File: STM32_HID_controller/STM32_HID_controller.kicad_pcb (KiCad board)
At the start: 2 copper layers, 249.9 x 110.4 mm, 49 parts, among them J1 USB_B_Micro, J2 Conn_01x04_Pin, J3 Conn_01x03_Pin, J5 Conn_01x03_Pin, SW1 SW_SPDT, SW10 SW_Push, SW11 SW_Push, SW14 SW_Push, SW2 SW_Push, SW3 SW_Push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

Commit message: Started flux
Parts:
- moved C6 4.89 mm to (149.2, 47.3), turned to 180 degrees
- moved C4 1.53 mm to (162.1, 41.3)
- moved C2 1.00 mm to (150.1, 29.5)
- moved C1 0.96 mm to (145.9, 40.7)
- moved C12 0.96 mm to (154.4, 49.7)
- moved C18 0.96 mm to (165.9, 37.7)
- moved C7 0.96 mm to (155.4, 45.2)
- moved FB1 0.96 mm to (159.7, 44.2)
- moved C10 0.96 mm to (165.4, 43.2)
- moved C15 0.96 mm to (156.9, 51.7)
- moved C16 0.96 mm to (159.9, 51.7)
- moved C17 0.96 mm to (165.9, 39.7)
- moved C3 0.96 mm to (161.4, 33.7)
- moved C5 0.96 mm to (149.4, 45.1)
- moved C8 0.96 mm to (157.9, 46.2)
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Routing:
- net vly: track 0.00 -> 78.6 mm
- net /SW_BOOT0: track 0.00 -> 21.1 mm
- net /SWDIO: track 0.00 -> 18.9 mm
- net /SWCLK: track 0.00 -> 16.7 mm
- net GND: track 0.00 -> 14.6 mm
- net +3.3V: track 0.00 -> 14.1 mm
- net /HSE_IN: track 0.00 -> 12.8 mm
- net /HSE_OUT: track 0.00 -> 9.72 mm
- net /USB_D-: track 0.00 -> 9.57 mm
- net /USB_D+: track 0.00 -> 9.49 mm
- net /BOOT0: track 0.00 -> 8.09 mm
- net vry: track 0.00 -> 6.77 mm
- net vrx: track 0.00 -> 6.19 mm
- net +3.3VA: track 0.00 -> 2.14 mm
- added copper zone on B.Cu, net GND

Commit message: Started flux
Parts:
- moved U4 159.0 mm to (218.8, 100.1)
- moved U5 153.6 mm to (70.1, 62.9)
- moved C16 20.5 mm to (141.7, 42.5), turned to 90 degrees
- moved SW1 18.1 mm to (133.9, 37.1), turned to -90 degrees
- moved C15 16.2 mm to (141.7, 46.1)
- moved C10 13.5 mm to (152.9, 48.4), turned to 0 degrees
- moved FB1 5.14 mm to (157.9, 49.0)
- moved C9 5.05 mm to (158.1, 50.9), turned to 0 degrees
- moved C11 2.63 mm to (149.3, 50.0)
- moved C12 2.63 mm to (151.8, 49.9)
- moved Y1 2.63 mm to (150.7, 53.0)
- moved U2 2.19 mm to (172.3, 30.8), turned to -90 degrees
- moved C5 2.18 mm to (147.3, 45.3)
- moved C6 2.18 mm to (147.0, 47.4)
- moved C8 1.39 mm to (157.0, 47.2), turned to 0 degrees
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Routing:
- net SCL: track 0.00 -> 315.1 mm
- net cs: track 0.00 -> 304.6 mm
- net jl: track 0.00 -> 214.3 mm
- net jr: track 0.00 -> 151.6 mm
- net vlx: track 0.00 -> 123.3 mm
- net vrx: track 6.19 -> 119.7 mm
- net zl: track 0.00 -> 102.6 mm
- net unconnected-(U1-PB7-Pad59): track 0.00 -> 92.6 mm
- net /A: track 0.00 -> 92.1 mm
- net /Y: track 0.00 -> 90.7 mm
- net /X: track 0.00 -> 88.1 mm
- net vry: track 6.77 -> 93.4 mm
- net r: track 0.00 -> 78.9 mm
- net SDO: track 0.00 -> 67.0 mm
- net SDI: track 0.00 -> 62.3 mm
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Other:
- outline, holes or cut-outs redrawn

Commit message: Started flux for left and right
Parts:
- removed R3: 10k, Resistor_SMD:R_0402_1005Metric
- removed U3: ADXL345, ADXL345:PQFN80P500X300X100-14N
- added U6: ADXL343, Package_LGA:LGA-14_3x5mm_P0.8mm_LayoutBorder1x6y, F.Cu at (112.2, 56.1)
- moved H2 14.3 mm to (51.1, 115.1)
- moved H4 12.5 mm to (51.1, 22.1)
- moved H6 7.00 mm to (277.1, 115.1)
- moved C17 5.70 mm to (164.2, 45.7)
- moved SW14 4.87 mm to (150.6, 69.8)
- moved C18 4.79 mm to (164.3, 42.6)
- moved C7 3.28 mm to (158.7, 45.6)
- moved C8 1.83 mm to (158.8, 47.1)
- moved C9 1.83 mm to (159.9, 50.8)
- moved FB1 1.83 mm to (159.7, 48.9)
- moved C1 1.33 mm to (145.0, 41.6)
- moved C4 0.90 mm to (161.5, 42.0)
- moved SW1 0.71 mm to (134.4, 36.6)
- moved C5 0.59 mm to (147.1, 44.8)
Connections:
- SW10 pad 1: /+ -> +
- SW11 pad 1: /- -> -
- SW14 pad 1: /ACC_control -> ACC_control
- SW2 pad 2: /home -> home
- SW3 pad 2: /capture -> capture
- SW6 pad 1: /A -> A
- SW7 pad 1: /B -> B
- SW8 pad 1: /X -> X
- SW9 pad 1: /Y -> Y
- U1 pad 11: unconnected-(U1-PC3-Pad11) -> cs
- U1 pad 22: cs -> jr
- U1 pad 23: unconnected-(U1-PA7-Pad23) -> B
- U1 pad 24: unconnected-(U1-PC4-Pad24) -> Y
- U1 pad 25: unconnected-(U1-PC5-Pad25) -> A
- U1 pad 26: unconnected-(U1-PB0-Pad26) -> X
- U1 pad 27: unconnected-(U1-PB1-Pad27) -> r
- U1 pad 28: unconnected-(U1-PB2-Pad28) -> zr
- U1 pad 29: SCL -> unconnected-(U1-PB10-Pad29)
- U1 pad 34: unconnected-(U1-PB13-Pad34) -> SCL
- U1 pad 35: l -> unconnected-(U1-PB14-Pad35)
- U1 pad 36: /ACC_control -> unconnected-(U1-PB15-Pad36)
- U1 pad 37: /home -> unconnected-(U1-PC6-Pad37)
- U1 pad 38: /capture -> unconnected-(U1-PC7-Pad38)
- U1 pad 39: zr -> unconnected-(U1-PC8-Pad39)
- U1 pad 40: zl -> unconnected-(U1-PC9-Pad40)
- U1 pad 41: jr -> unconnected-(U1-PA8-Pad41)
- U1 pad 42: jl -> unconnected-(U1-PA9-Pad42)
- U1 pad 43: r -> unconnected-(U1-PA10-Pad43)
- U1 pad 51: unconnected-(U1-PC10-Pad51) -> l
- U1 pad 52: unconnected-(U1-PC11-Pad52) -> zl
- U1 pad 55: /A -> jl
- U1 pad 56: /B -> home
- U1 pad 57: /X -> +
- U1 pad 58: /Y -> unconnected-(U1-PB6-Pad58)
- U1 pad 61: /+ -> -
- U1 pad 62: /- -> capture
- U1 pad 8: unconnected-(U1-PC0-Pad8) -> ACC_control
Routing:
- net +: track 0.00 -> 293.3 mm
- net home: track 0.00 -> 273.7 mm
- net capture: track 0.00 -> 238.1 mm
- net -: track 0.00 -> 231.8 mm
- net cs: track 304.6 -> 78.2 mm
- net SCL: track 315.1 -> 530.5 mm
- net jl: track 214.3 -> 103.3 mm
- net A: track 0.00 -> 110.2 mm
- net B: track 0.00 -> 96.3 mm
- net unconnected-(U1-PB7-Pad59): track 92.6 -> 0.00 mm
- net /A: track 92.1 -> 0.00 mm
- net /Y: track 90.7 -> 0.00 mm
- net /X: track 88.1 -> 0.00 mm
- net X: track 0.00 -> 82.9 mm
- net jr: track 151.6 -> 82.3 mm
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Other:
- board size 249.9 x 110.4 mm -> 237.3 x 103.7 mm

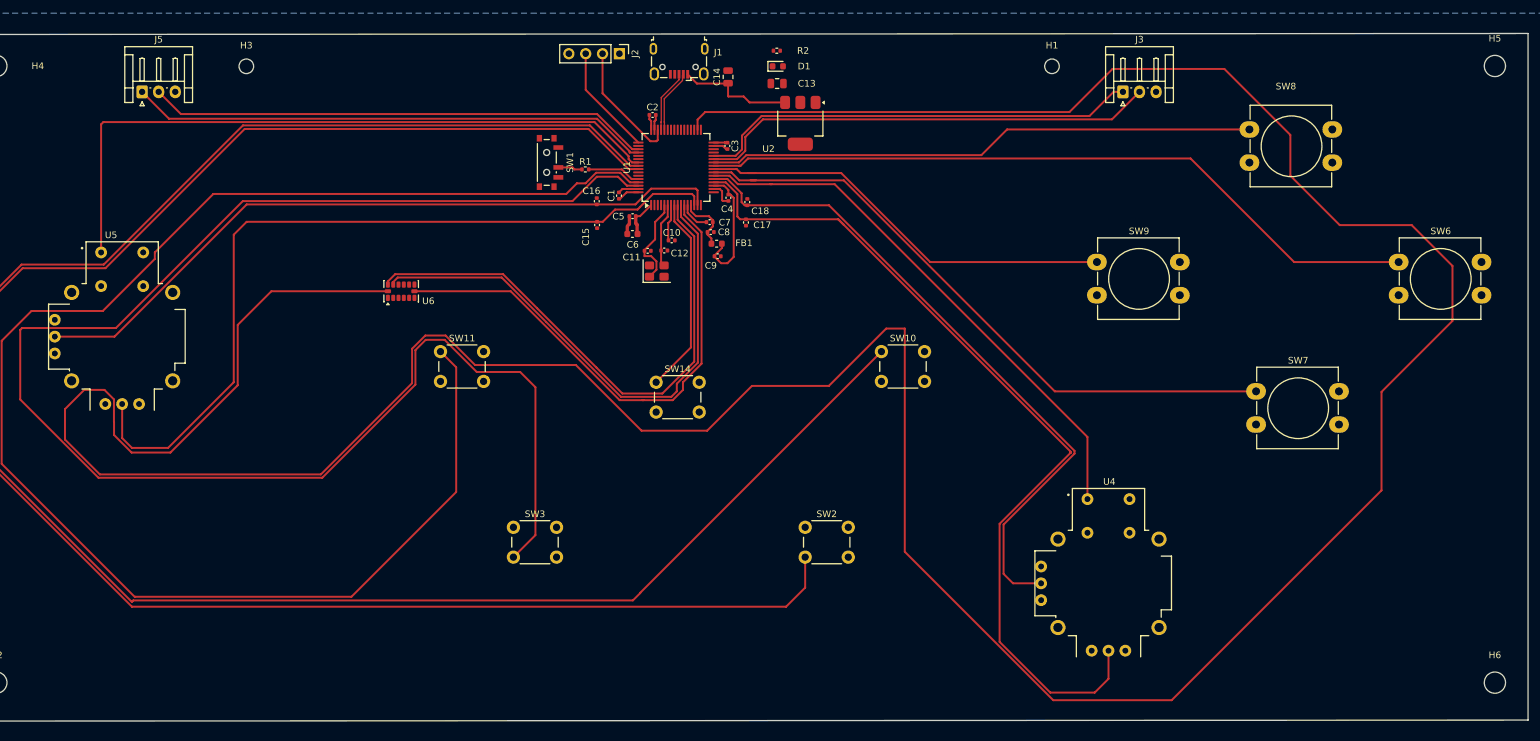
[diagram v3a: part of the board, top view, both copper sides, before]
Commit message: added gnd vias shortend sclk
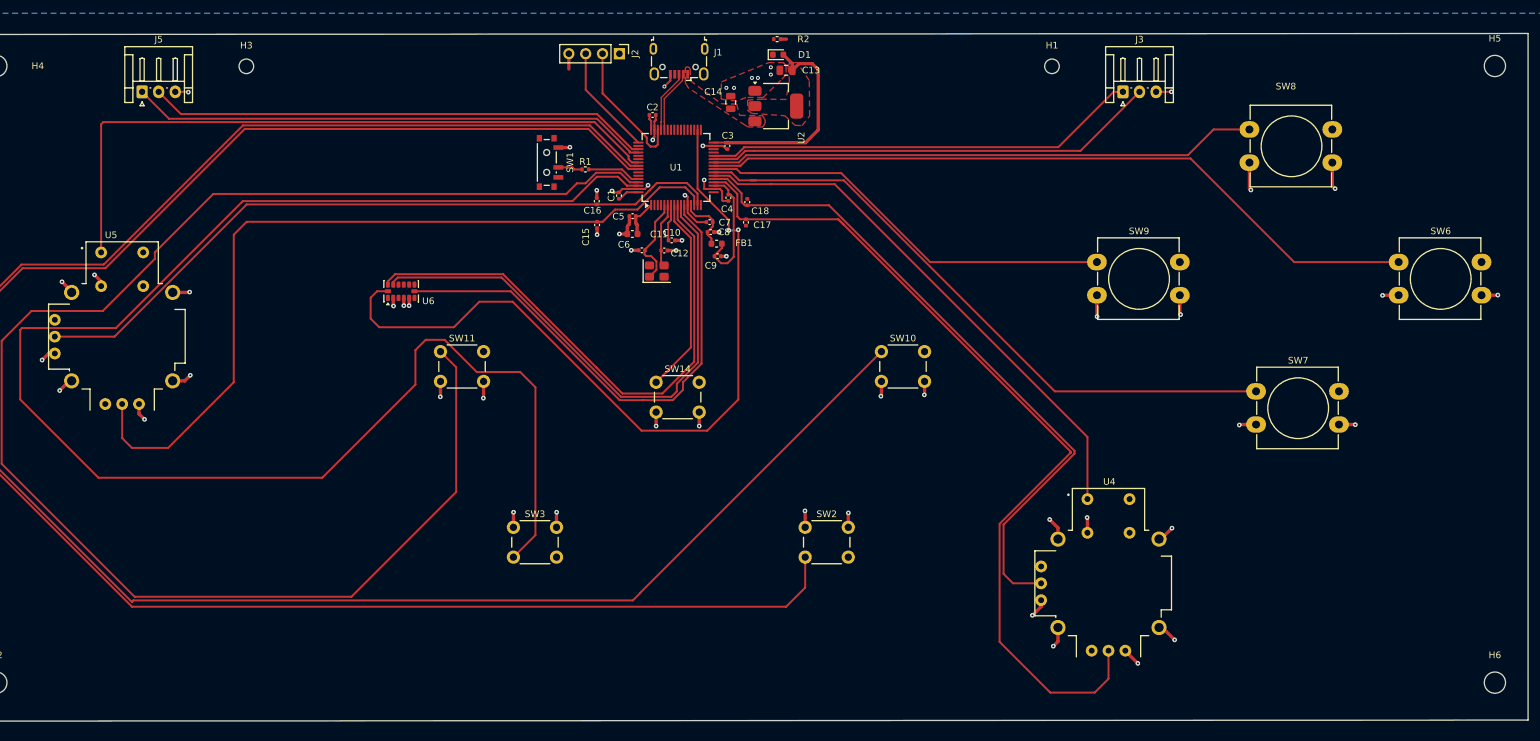
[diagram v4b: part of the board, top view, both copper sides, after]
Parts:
- moved U2 4.52 mm to (168.7, 28.1), turned to 0 degrees
- moved C14 3.87 mm to (161.8, 27.6)
- moved C13 2.41 mm to (170.2, 22.8)
- moved D1 1.75 mm to (169.0, 20.4)
- moved R2 1.75 mm to (168.8, 18.1)
- moved C11 0.88 mm to (148.4, 49.9), turned to 180 degrees
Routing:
- net SCL: track 530.5 -> 118.0 mm, vias 0 -> 2
- net GND: track 18.9 -> 137.8 mm, vias 0 -> 59
- net +3.3V: track 32.9 -> 64.5 mm
- net VBUS: track 17.6 -> 0.00 mm
- net /SWDIO: track 18.9 -> 20.4 mm
- net r: track 69.7 -> 68.4 mm
- net zr: track 66.9 -> 65.7 mm
- net vlx: track 122.4 -> 123.2 mm
- added copper zone on F.Cu, net +3.3V
- added copper zone on F.Cu, net GND
- added copper zone on F.Cu, net VBUS

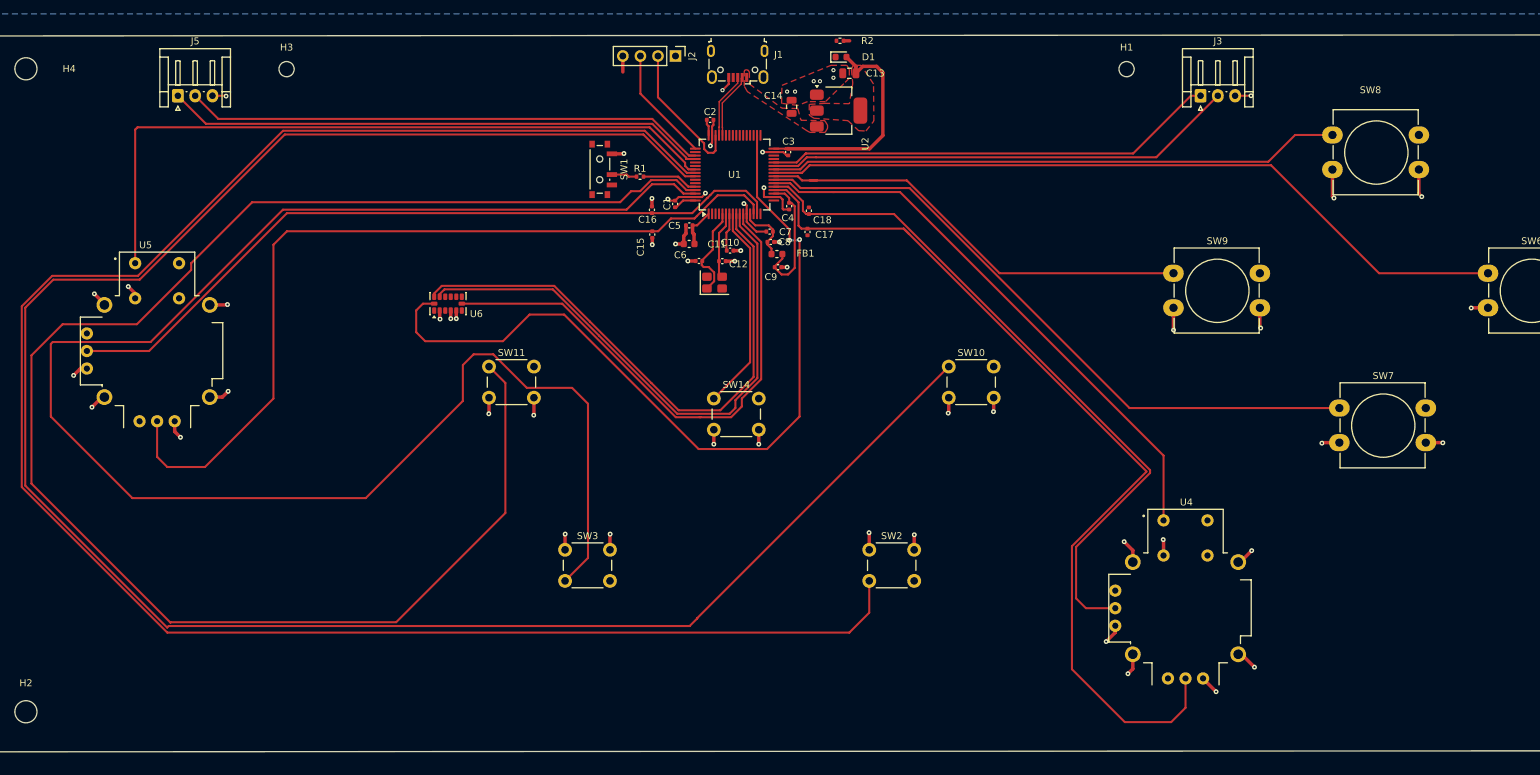
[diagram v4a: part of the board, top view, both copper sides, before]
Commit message: added gnd vias shortend sclk
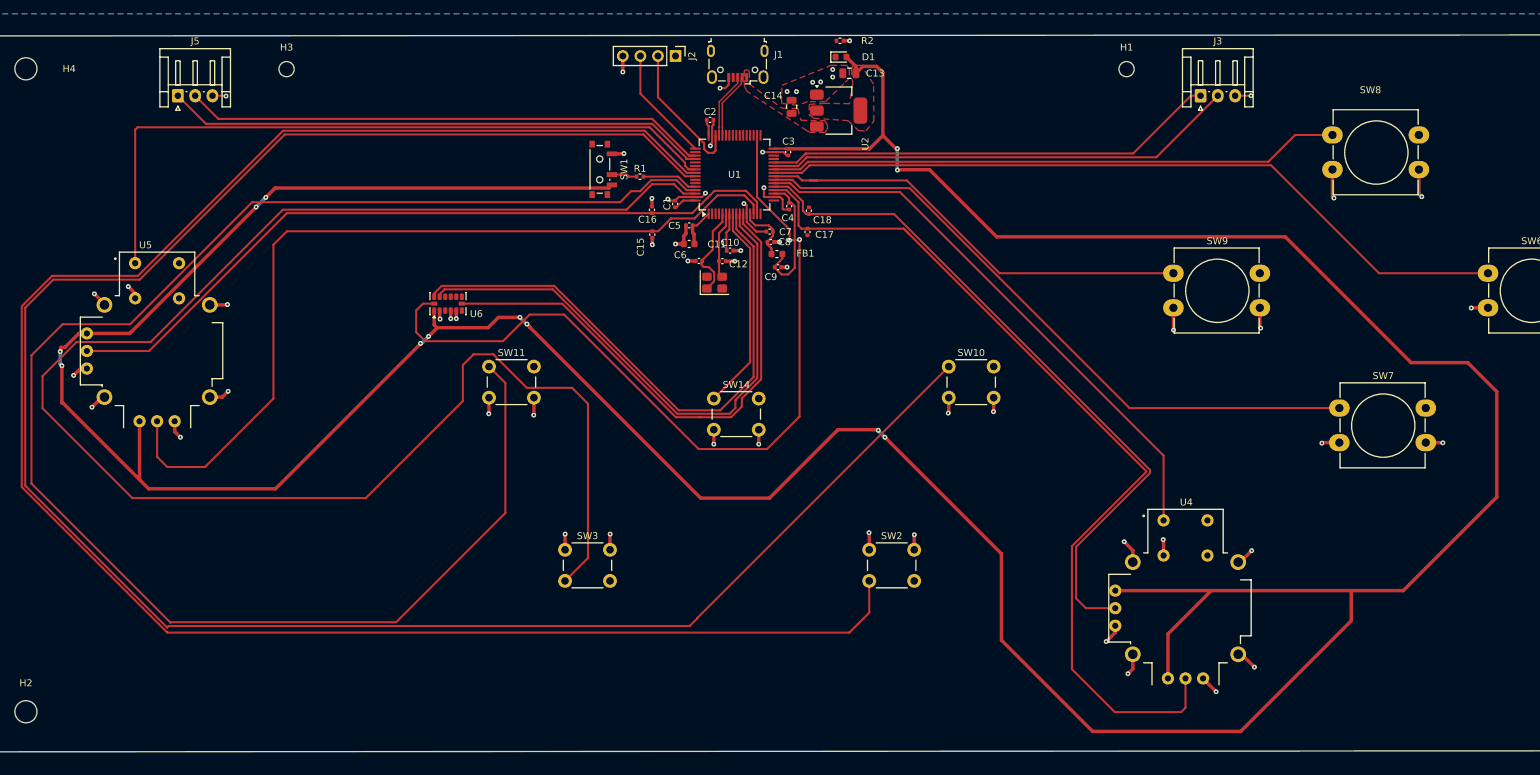
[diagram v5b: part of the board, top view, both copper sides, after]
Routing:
- net +3.3V: track 64.5 -> 624.2 mm, vias 0 -> 12
- net vrx: track 131.7 -> 130.5 mm
- net capture: track 238.1 -> 237.0 mm
- net GND: track 137.8 -> 138.6 mm, vias 59 -> 55
- net -: track 231.8 -> 231.3 mm
- net (no net): track 0.00 -> 0.10 mm, vias 0 -> 6
